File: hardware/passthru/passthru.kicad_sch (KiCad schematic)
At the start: 75 parts, among them J1 ARM_SWD, J2 RJ45_LED_Shielded, J3 Screw_Terminal_01x02, Q1 Q_PMOS_DGS, Q2 Q_PMOS_DGS, U1 EFM32GG11B8xx, U2 KSZ8081RND, U3 LM5085, U4 TPS2375-1

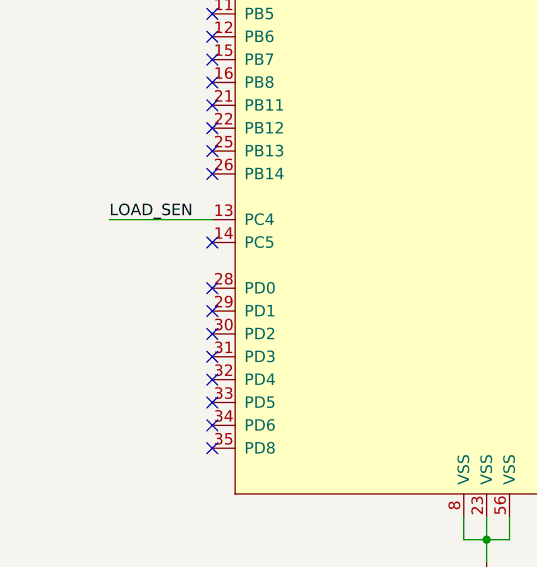
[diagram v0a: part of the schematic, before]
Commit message: passthru: add decoupling cap to load sense signal
Unsure if this is needed, but it should help dampen any ringing
present in the signal.
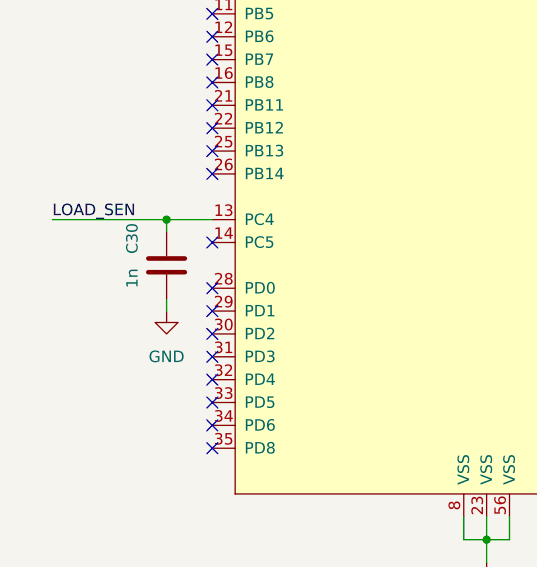
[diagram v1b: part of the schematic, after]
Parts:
- added C30: 1n, symbol Device:C
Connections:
- net GND: now also C30.2
- net LOAD_SEN: now also C30.1
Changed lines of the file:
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@@
   (junction (at 204.47 22.86) (diameter 0) (color 0 0 0 0)
   )
+  (junction (at 30.48 157.48) (diameter 0) (color 0 0 0 0)
+  )
   (junction (at 170.18 139.7) (diameter 0) (color 0 0 0 0)
   )
@@
     (stroke (width 0) (type default) (color 0 0 0 0))
   )
+  (wire (pts (xy 30.48 157.48) (xy 30.48 158.75))
+    (stroke (width 0) (type default) (color 0 0 0 0))
+  )
   (wire (pts (xy 212.09 30.48) (xy 212.09 35.56))
     (stroke (width 0) (type default) (color 0 0 0 0))
@@
     (stroke (width 0) (type default) (color 0 0 0 0))
   )
+  (wire (pts (xy 30.48 166.37) (xy 30.48 167.64))
+    (stroke (width 0) (type default) (color 0 0 0 0))
+  )
   (wire (pts (xy 245.11 22.86) (xy 256.54 22.86))
     (stroke (width 0) (type default) (color 0 0 0 0))
@@
     (stroke (width 0) (type default) (color 0 0 0 0))
   )
-  (wire (pts (xy 24.13 157.48) (xy 35.56 157.48))
+  (wire (pts (xy 17.78 157.48) (xy 30.48 157.48))
     (stroke (width 0) (type default) (color 0 0 0 0))
   )
@@
     (stroke (width 0) (type default) (color 0 0 0 0))
   )
+  (wire (pts (xy 30.48 157.48) (xy 35.56 157.48))
+    (stroke (width 0) (type default) (color 0 0 0 0))
+  )
   (wire (pts (xy 25.4 132.08) (xy 35.56 132.08))
     (stroke (width 0) (type default) (color 0 0 0 0))
@@
     (effects (font (size 1.27 1.27)) (justify left bottom))
   )
-  (label "LOAD_SEN" (at 24.13 157.48 0)
+  (label "LOAD_SEN" (at 17.78 157.48 0)
     (effects (font (size 1.27 1.27)) (justify left bottom))
   )
@@
     (pin "1")
   )
+  (symbol (lib_id "Device:C") (at 30.48 162.56 0) (mirror y) (unit 1)
+    (in_bom yes) (on_board yes)
+    (property "Reference" "C30" (id 0) (at 26.67 161.2899 90)
+      (effects (font (size 1.27 1.27)) (justify left))
+    )
+    (property "Value" "1n" (id 1) (at 26.67 165.1 90)
+      (effects (font (size 1.27 1.27)) (justify left))
+    )
+    (property "Footprint" "" (id 2) (at 29.5148 166.37 0)
+      (effects (font (size 1.27 1.27)) hide)
+    )
+    (property "Datasheet" "~" (id 3) (at 30.48 162.56 0)
+      (effects (font (size 1.27 1.27)) hide)
+    )
+    (pin "1")
+    (pin "2")
+  )
   (symbol (lib_id "Device:C") (at 229.87 102.87 0) (unit 1)
     (in_bom yes) (on_board yes)
@@
     (pin "1")
   )
+  (symbol (lib_id "power:GND") (at 30.48 167.64 0) (unit 1)
+    (in_bom yes) (on_board yes) (fields_autoplaced)
+    (property "Reference" "#PWR051" (id 0) (at 30.48 173.99 0)
+      (effects (font (size 1.27 1.27)) hide)
+    )
+    (property "Value" "GND" (id 1) (at 30.48 172.72 0))
+    (property "Footprint" "" (id 2) (at 30.48 167.64 0)
+      (effects (font (size 1.27 1.27)) hide)
+    )
+    (property "Datasheet" "" (id 3) (at 30.48 167.64 0)
+      (effects (font (size 1.27 1.27)) hide)
+    )
+    (pin "1")
+  )
   (symbol (lib_id "power:PWR_FLAG") (at 135.89 26.67 0) (unit 1)
     (in_bom yes) (on_board yes)
@@
       (reference "#PWR050") (unit 1) (value "+3V3") (footprint "")
     )
+    (path "/95dff5ea-28e0-4ad8-b7f4-dce50f7c76b3"
+      (reference "#PWR051") (unit 1) (value "GND") (footprint "")
+    )
     (path "/c61db7ba-41b9-4169-bb6f-11722db31004"
       (reference "C1") (unit 1) (value "0u1") (footprint "")
@@
       (reference "C29") (unit 1) (value "1u") (footprint "")
     )
+    (path "/44d7f415-7f4a-47ad-ba9e-f54f5a3acb9a"
+      (reference "C30") (unit 1) (value "1n") (footprint "")
+    )
     (path "/ca2774aa-b255-4c6c-bae3-4d11c27b5cce"

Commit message: passthru: assign the rest of the footprints
Just going with 0603s for everything except the shut resistor, which I
already have stocked.
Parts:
- C1, C10, C11, C15, C18, C2, C23, C24, C25, C26, C27, C28, C29, C3, C30, C4, C5, C6, C7, C8, C9: footprint (none) -> Capacitor_SMD:C_0603_1608Metric_Pad1.08x0.95mm_HandSolder
- R1, R11, R13, R14, R16, R17, R19, R2, R20, R21, R3, R4, R5, R9: footprint (none) -> Resistor_SMD:R_0603_1608Metric_Pad0.98x0.95mm_HandSolder
- R18: footprint (none) -> Resistor_SMD:R_0805_2012Metric_Pad1.20x1.40mm_HandSolder

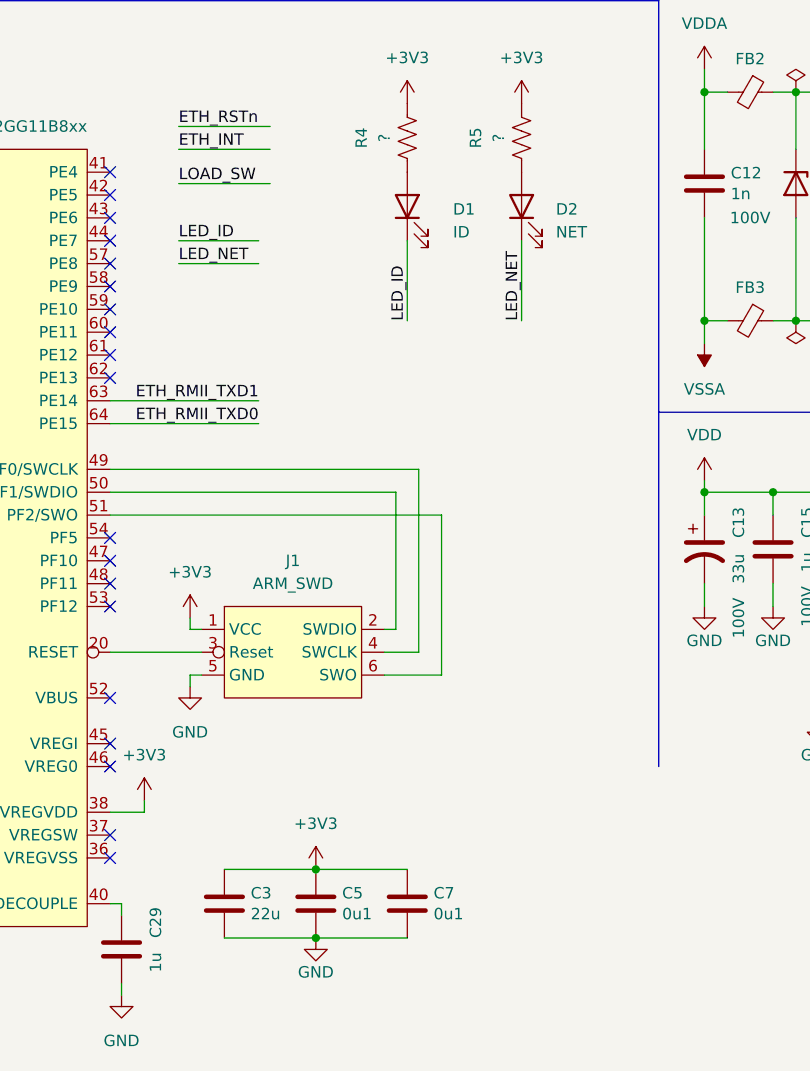
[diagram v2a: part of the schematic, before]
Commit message: passthru: add driver circuit for load switch
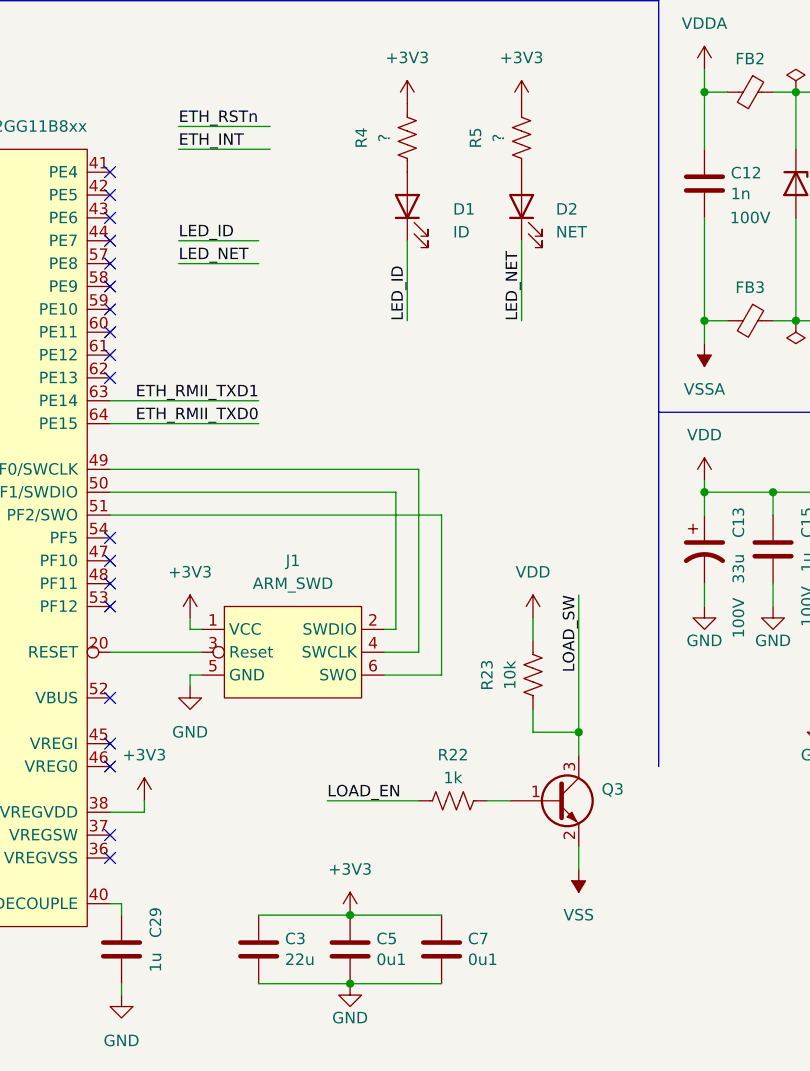
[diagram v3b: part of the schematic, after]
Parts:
- added Q3: Q_NPN_BEC, Package_TO_SOT_SMD:SOT-23, symbol Device:Q_NPN_BEC
- added R22: 1k, Resistor_SMD:R_0603_1608Metric_Pad0.98x0.95mm_HandSolder, symbol Device:R_US
- added R23: 10k, Resistor_SMD:R_0603_1608Metric_Pad0.98x0.95mm_HandSolder, symbol Device:R_US
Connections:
- net LOAD_SW: now also Q3.3 (C), R23.1
- net VDD: now also R23.2
- net VSS: now also Q3.2 (E)
- new net: Q3.1 (B), R22.2
- new net LOAD_EN: R22.1
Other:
- moved on the sheet: C3, C5, C7

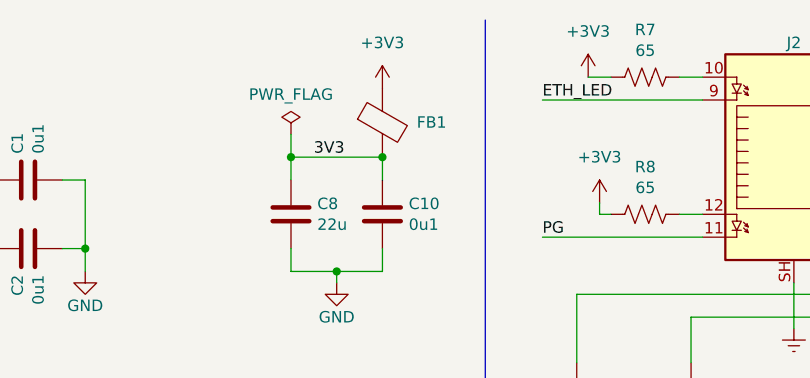
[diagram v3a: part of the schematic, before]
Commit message: passthru: assign the rest of the footprints
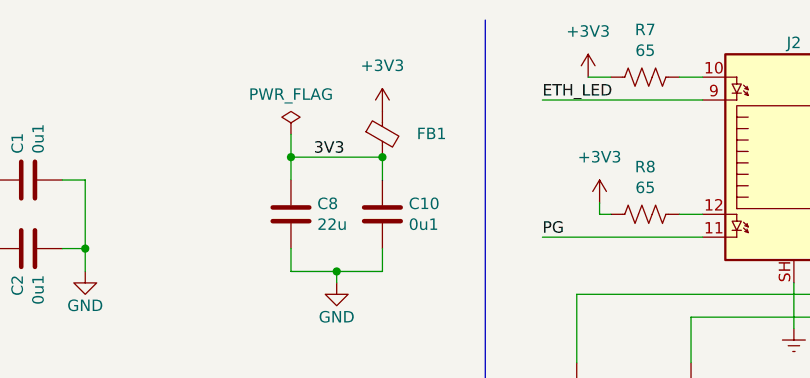
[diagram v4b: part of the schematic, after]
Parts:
- D5: footprint (none) -> Diode_SMD:D_SOD-323F
- FB1: value FerriteBead -> Ferrite_Bead_Small; footprint (none) -> Inductor_SMD:L_0603_1608Metric_Pad1.05x0.95mm_HandSolder; symbol Device:FerriteBead -> Device:FerriteBead_Small
- FB2, FB3: footprint (none) -> Inductor_SMD:L_0603_1608Metric_Pad1.05x0.95mm_HandSolder
- L1: footprint (none) -> Inductor_SMD:L_1210_3225Metric_Pad1.42x2.65mm_HandSolder
- Q1, Q2: footprint (none) -> Package_SO:PowerPAK_SO-8_Single
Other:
- moved on the sheet: FB1
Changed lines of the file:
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@@
       (effects (font (size 1.27 1.27)) hide)
     )
-    (property "Footprint" "" (id 2) (at 167.64 118.872 90)
+    (property "Footprint" "Inductor_SMD:L_0603_1608Metric_Pad1.05x0.95mm_HandSolder" (id 2) (at 167.64 118.872 90)
       (effects (font (size 1.27 1.27)) hide)
     )
@@
       (effects (font (size 1.27 1.27)) (justify left) hide)
     )
-    (property "Footprint" "" (id 2) (at 237.49 151.13 0)
+    (property "Footprint" "Diode_SMD:D_SOD-323F" (id 2) (at 237.49 151.13 0)
       (effects (font (size 1.27 1.27)) hide)
     )
@@
     (pin "2")
   )
-  (symbol (lib_id "Device:FerriteBead") (at 146.05 25.4 0) (unit 1)
-    (in_bom yes) (on_board yes) (fields_autoplaced)
-    (property "Reference" "FB1" (id 0) (at 149.86 25.3491 0)
-      (effects (font (size 1.27 1.27)) (justify left))
-    )
-    (property "Value" "FerriteBead" (id 1) (at 149.86 26.6191 0)
+  (symbol (lib_id "Device:FerriteBead_Small") (at 146.05 26.67 0) (unit 1)
+    (in_bom yes) (on_board yes) (fields_autoplaced)
+    (property "Reference" "FB1" (id 0) (at 149.86 26.6191 0)
+      (effects (font (size 1.27 1.27)) (justify left))
+    )
+    (property "Value" "Ferrite_Bead_Small" (id 1) (at 149.86 27.8891 0)
       (effects (font (size 1.27 1.27)) (justify left) hide)
     )
-    (property "Footprint" "" (id 2) (at 144.272 25.4 90)
-      (effects (font (size 1.27 1.27)) hide)
-    )
-    (property "Datasheet" "~" (id 3) (at 146.05 25.4 0)
+    (property "Footprint" "Inductor_SMD:L_0603_1608Metric_Pad1.05x0.95mm_HandSolder" (id 2) (at 144.272 26.67 90)
+      (effects (font (size 1.27 1.27)) hide)
+    )
+    (property "Datasheet" "~" (id 3) (at 146.05 26.67 0)
       (effects (font (size 1.27 1.27)) hide)
     )
@@
       (effects (font (size 1.27 1.27)) (justify left) hide)
     )
-    (property "Footprint" "" (id 2) (at 234.95 137.16 0)
+    (property "Footprint" "Package_SO:PowerPAK_SO-8_Single" (id 2) (at 234.95 137.16 0)
       (effects (font (size 1.27 1.27)) hide)
     )
@@
       (effects (font (size 1.27 1.27)) hide)
     )
-    (property "Footprint" "" (id 2) (at 167.64 93.472 90)
+    (property "Footprint" "Inductor_SMD:L_0603_1608Metric_Pad1.05x0.95mm_HandSolder" (id 2) (at 167.64 93.472 90)
       (effects (font (size 1.27 1.27)) hide)
     )
@@
     (pin "2")
   )
-  (symbol (lib_id "power:+3V3") (at 146.05 21.59 0) (unit 1)
-    (in_bom yes) (on_board yes) (fields_autoplaced)
-    (property "Reference" "#PWR021" (id 0) (at 146.05 25.4 0)
-      (effects (font (size 1.27 1.27)) hide)
-    )
-    (property "Value" "+3V3" (id 1) (at 146.05 16.51 0))
-    (property "Footprint" "" (id 2) (at 146.05 21.59 0)
-      (effects (font (size 1.27 1.27)) hide)
-    )
-    (property "Datasheet" "" (id 3) (at 146.05 21.59 0)
+  (symbol (lib_id "power:+3V3") (at 146.05 24.13 0) (unit 1)
+    (in_bom yes) (on_board yes) (fields_autoplaced)
+    (property "Reference" "#PWR021" (id 0) (at 146.05 27.94 0)
+      (effects (font (size 1.27 1.27)) hide)
+    )
+    (property "Value" "+3V3" (id 1) (at 146.05 19.05 0))
+    (property "Footprint" "" (id 2) (at 146.05 24.13 0)
+      (effects (font (size 1.27 1.27)) hide)
+    )
+    (property "Datasheet" "" (id 3) (at 146.05 24.13 0)
       (effects (font (size 1.27 1.27)) hide)
     )
@@
       (effects (font (size 1.27 1.27)) hide)
     )
-    (property "Footprint" "" (id 2) (at 236.22 97.79 0)
+    (property "Footprint" "Package_SO:PowerPAK_SO-8_Single" (id 2) (at 236.22 97.79 0)
       (effects (font (size 1.27 1.27)) hide)
     )
@@
     (property "Reference" "L1" (id 0) (at 243.84 133.35 90))
     (property "Value" "15u" (id 1) (at 243.84 135.89 90))
-    (property "Footprint" "" (id 2) (at 243.84 139.7 0)
+    (property "Footprint" "Inductor_SMD:L_1210_3225Metric_Pad1.42x2.65mm_HandSolder" (id 2) (at 243.84 139.7 0)
       (effects (font (size 1.27 1.27)) hide)
     )
@@
     )
     (path "/19245aa1-3585-4306-802e-34b2720c21bf"
-      (reference "D5") (unit 1) (value "D_Schottky") (footprint "")
+      (reference "D5") (unit 1) (value "D_Schottky") (footprint "Diode_SMD:D_SOD-323F")
     )
     (path "/9b2b1fee-ecec-4d3e-b91f-8bf5b17cdc5b"
@@
     )
     (path "/300f7308-210e-43a3-a869-5f6d3674a894"
-      (reference "FB1") (unit 1) (value "FerriteBead") (footprint "")
+      (reference "FB1") (unit 1) (value "Ferrite_Bead_Small") (footprint "Inductor_SMD:L_0603_1608Metric_Pad1.05x0.95mm_HandSolder")
     )
     (path "/70d69380-7dfe-4d0b-aa69-88fd972c78d8"
-      (reference "FB2") (unit 1) (value "Ferrite_Bead_Small") (footprint "")
+      (reference "FB2") (unit 1) (value "Ferrite_Bead_Small") (footprint "Inductor_SMD:L_0603_1608Metric_Pad1.05x0.95mm_HandSolder")
     )
     (path "/0252ba3b-68cd-4338-af7e-05143e6d8ddb"
-      (reference "FB3") (unit 1) (value "Ferrite_Bead_Small") (footprint "")
+      (reference "FB3") (unit 1) (value "Ferrite_Bead_Small") (footprint "Inductor_SMD:L_0603_1608Metric_Pad1.05x0.95mm_HandSolder")
     )
     (path "/8913f3cf-c979-4a91-9f24-c81e7a7c460c"
@@
     )
     (path "/f10a8ce2-1323-49de-b979-aea192421d3f"
-      (reference "L1") (unit 1) (value "15u") (footprint "")
+      (reference "L1") (unit 1) (value "15u") (footprint "Inductor_SMD:L_1210_3225Metric_Pad1.42x2.65mm_HandSolder")
     )
     (path "/3b171c12-23a9-40c9-8b4b-a2865c498c23"
-      (reference "Q1") (unit 1) (value "Q_PMOS_DGS") (footprint "")
+      (reference "Q1") (unit 1) (value "Q_PMOS_DGS") (footprint "Package_SO:PowerPAK_SO-8_Single")
     )
     (path "/d50e64c1-165e-4e88-931e-7e1d4303054e"
-      (reference "Q2") (unit 1) (value "Q_PMOS_DGS") (footprint "")
+      (reference "Q2") (unit 1) (value "Q_PMOS_DGS") (footprint "Package_SO:PowerPAK_SO-8_Single")
     )
     (path "/5ace4dd3-8bbf-416c-b527-4a320e0eb289"
-      (reference "Q3") (unit 1) (value "Q_NPN_BCE") (footprint "Package_TO_SOT_SMD:SOT-23")
+      (reference "Q3") (unit 1) (value "Q_NPN_BEC") (footprint "Package_TO_SOT_SMD:SOT-23")
     )
     (path "/3c762da0-acfa-46d8-ad01-d3d1533c6098"

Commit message: passthru: fix test point values
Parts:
- TP2: value VB -> VDD
- TP3: value 12V -> VSS
- TP5: value GND -> 3V3
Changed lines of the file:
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@@
       (effects (font (size 1.27 1.27)) (justify right))
     )
-    (property "Value" "GND" (id 1) (at 253.873 134.9248 90)
+    (property "Value" "3V3" (id 1) (at 253.873 134.9248 90)
       (effects (font (size 1.27 1.27)) (justify left) hide)
     )
@@
       (effects (font (size 1.27 1.27)) (justify right))
     )
-    (property "Value" "12V" (id 1) (at 180.467 125.4252 90)
+    (property "Value" "VSS" (id 1) (at 180.467 125.4252 90)
       (effects (font (size 1.27 1.27)) (justify left) hide)
     )
@@
     (in_bom yes) (on_board yes)
     (property "Reference" "TP2" (id 0) (at 181.61 89.535 0))
-    (property "Value" "VB" (id 1) (at 182.753 90.4748 90)
+    (property "Value" "VDD" (id 1) (at 182.753 90.4748 90)
       (effects (font (size 1.27 1.27)) (justify left) hide)
     )
@@
     )
     (path "/6f6d20a5-826b-4b81-bdd1-fceaa2b970c2"
-      (reference "TP2") (unit 1) (value "VB") (footprint "TestPoint:TestPoint_Loop_D1.80mm_Drill1.0mm_Beaded")
+      (reference "TP2") (unit 1) (value "VDD") (footprint "TestPoint:TestPoint_Loop_D1.80mm_Drill1.0mm_Beaded")
     )
     (path "/0f41e8ee-d677-4198-a5d1-8c2a582d292e"
-      (reference "TP3") (unit 1) (value "12V") (footprint "TestPoint:TestPoint_Loop_D1.80mm_Drill1.0mm_Beaded")
+      (reference "TP3") (unit 1) (value "VSS") (footprint "TestPoint:TestPoint_Loop_D1.80mm_Drill1.0mm_Beaded")
     )
     (path "/13215c1d-73d1-47c4-86e8-93ec70674c3e"
@@
     )
     (path "/0df6d917-84df-40b5-b173-fe738754d239"
-      (reference "TP5") (unit 1) (value "GND") (footprint "TestPoint:TestPoint_Loop_D1.80mm_Drill1.0mm_Beaded")
+      (reference "TP5") (unit 1) (value "3V3") (footprint "TestPoint:TestPoint_Loop_D1.80mm_Drill1.0mm_Beaded")
     )
     (path "/20bbebde-9b3d-4535-896f-7dc21cb46df2"
